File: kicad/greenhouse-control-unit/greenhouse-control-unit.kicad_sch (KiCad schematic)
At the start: 69 parts, among them J1 Pluggable_Terminal_01x02, J10 Molex_KK-254_01x10, J10_LittleBuck1 Conn_01x01_Female, J11_LittleBuck1 Conn_01x01_Female, J12_BigBuck1 Conn_01x01_Female, J13_BigBuck1 Conn_01x01_Female, J14_LittleBuck1 Conn_01x01_Female, J15_LittleBuck1 Conn_01x01_Female, J2 Pluggable_Terminal_01x02, J3 Pluggable_Terminal_01x02, J4 Molex_KK-254_01x08, J5 Conn_01x10_Female, J6 Conn_01x10_Female, J6_BigBuck1 Conn_01x01_Female, J7 Conn_01x15_Female, J7_BigBuck1 Conn_01x01_Female, J8 Conn_01x15_Female, J9 Molex_KK-396_01x16, Q1 2N7000, Q10 IRLB8721PBF, Q11 IRLB8721PBF, Q2 2N7000, Q3 2N7000, Q4 IRLB8721PBF, Q5 IRLB8721PBF, Q6 IRLB8721PBF, Q7 IRLB8721PBF, Q8 IRLB8721PBF, Q9 IRLB8721PBF, U1 74HC595, U2 74HC595

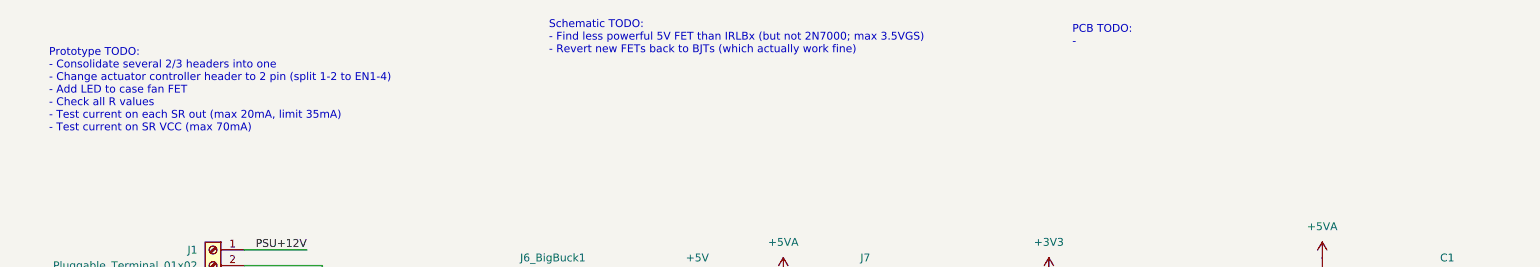
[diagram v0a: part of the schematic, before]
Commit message: Updated TODO's to use 2N7x's properly
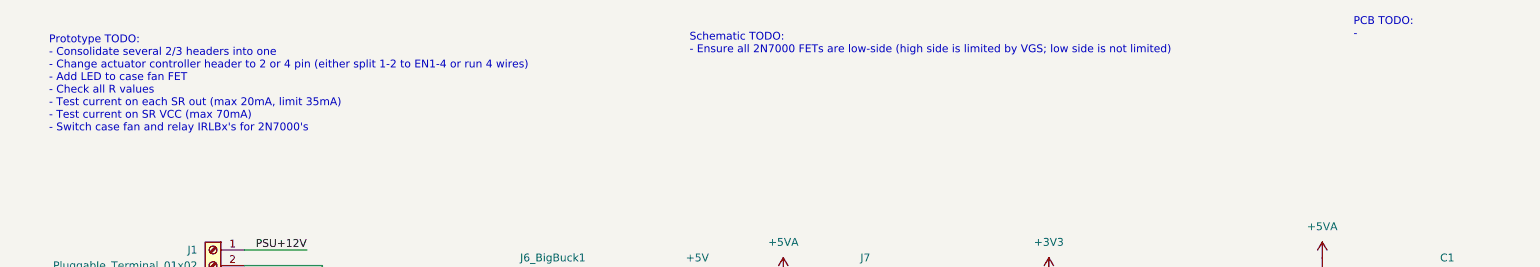
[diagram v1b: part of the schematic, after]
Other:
- note added: "Prototype TODO: - Consolidate several 2/3 headers into one - Change actuator controller header to 2 or 4 pin (either split 1-2 to EN1-4 or run 4 wires) - Add LED to case fan FET - Check all R values - Test current on each SR out (max 20mA, limit 35mA) - Test current on SR VCC (max 70mA) - Switch case fan and relay IRLBx's for 2N7000's"
- note added: "Schematic TODO: - Ensure all 2N7000 FETs are low-side (high side is limited by VGS; low side is not limited)"
- note removed: "Prototype TODO: - Consolidate several 2/3 headers into one - Change actuator controller header to 2 pin (split 1-2 to EN1-4) - Add LED to case fan FET - Check all R values - Test current on each SR out (max 20mA, limit 35mA) - Test current on SR VCC (max 70mA)"
- note removed: "Schematic TODO: - Find less powerful 5V FET than IRLBx (but not 2N7000; max 3.5VGS) - Revert new FETs back to BJTs (which actually work fine)"
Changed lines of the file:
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@@
     (effects (font (size 1.27 1.27)) (justify left bottom))
   )
-  (text "PCB TODO:\n- " (at 193.04 22.86 0)
+  (text "PCB TODO:\n- " (at 238.76 21.59 0)
     (effects (font (size 1.27 1.27)) (justify left bottom))
   )
@@
     (effects (font (size 1.27 1.27)) (justify left bottom))
   )
-  (text "Schematic TODO:\n- Find less powerful 5V FET than IRLBx (but not 2N7000; max 3.5VGS)\n- Revert new FETs back to BJTs (which actually work fine)"
-    (at 107.95 24.13 0)
+  (text "Schematic TODO:\n- Ensure all 2N7000 FETs are low-side (high side is limited by VGS; low side is not limited)\n"
+    (at 130.81 24.13 0)
     (effects (font (size 1.27 1.27)) (justify left bottom))
   )
-  (text "Prototype TODO:\n- Consolidate several 2/3 headers into one\n- Change actuator controller header to 2 pin (split 1-2 to EN1-4)\n- Add LED to case fan FET\n- Check all R values\n- Test current on each SR out (max 20mA, limit 35mA)\n- Test current on SR VCC (max 70mA)"
+  (text "Prototype TODO:\n- Consolidate several 2/3 headers into one\n- Change actuator controller header to 2 or 4 pin (either split 1-2 to EN1-4 or run 4 wires)\n- Add LED to case fan FET\n- Check all R values\n- Test current on each SR out (max 20mA, limit 35mA)\n- Test current on SR VCC (max 70mA)\n- Switch case fan and relay IRLBx's for 2N7000's"
     (at 26.67 36.83 0)
     (effects (font (size 1.27 1.27)) (justify left bottom))

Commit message: Update TODO and ignore file
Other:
- note added: "Schematic TODO: - Ensure all 2N7000 FETs are low-side (high side is limited by VGS; low side is not limited) - Resistors on SR inputs to prevent parasite power? Maybe make diode redundant?"
- note removed: "Schematic TODO: - Ensure all 2N7000 FETs are low-side (high side is limited by VGS; low side is not limited)"
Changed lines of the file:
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@@
     (effects (font (size 1.27 1.27)) (justify left bottom))
   )
-  (text "PCB TODO:\n- " (at 238.76 21.59 0)
+  (text "PCB TODO:\n- " (at 240.03 24.13 0)
     (effects (font (size 1.27 1.27)) (justify left bottom))
   )
@@
     (effects (font (size 1.27 1.27)) (justify left bottom))
   )
-  (text "Schematic TODO:\n- Ensure all 2N7000 FETs are low-side (high side is limited by VGS; low side is not limited)\n"
-    (at 130.81 24.13 0)
+  (text "Schematic TODO: \n- Ensure all 2N7000 FETs are low-side (high side is limited by VGS; low side is not limited)\n- Resistors on SR inputs to prevent parasite power? Maybe make diode redundant?"
+    (at 132.08 26.67 0)
     (effects (font (size 1.27 1.27)) (justify left bottom))
   )
@@
     )
   )
-  (symbol (lib_id "power:+5V") (at 120.65 217.17 0) (unit 1)
-    (in_bom yes) (on_board yes) (fields_autoplaced)
-    (property "Reference" "#PWR07" (id 0) (at 120.65 220.98 0)
-      (effects (font (size 1.27 1.27)) hide)
-    )
-    (property "Value" "+5V" (id 1) (at 120.65 212.09 0))
-    (property "Footprint" "" (id 2) (at 120.65 217.17 0)
-      (effects (font (size 1.27 1.27)) hide)
-    )
-    (property "Datasheet" "" (id 3) (at 120.65 217.17 0)
-      (effects (font (size 1.27 1.27)) hide)
-    )
-    (pin "1")
-  )
   (symbol (lib_id "power:GND") (at 233.68 243.84 0) (unit 1)
     (in_bom yes) (on_board yes) (fields_autoplaced)
@@
     (pin "2")
   )
+  (symbol (lib_id "power:+5V") (at 120.65 217.17 0) (unit 1)
+    (in_bom yes) (on_board yes) (fields_autoplaced)
+    (property "Reference" "#PWR?" (id 0) (at 120.65 220.98 0)
+      (effects (font (size 1.27 1.27)) hide)
+    )
+    (property "Value" "+5V" (id 1) (at 120.65 212.09 0))
+    (property "Footprint" "" (id 2) (at 120.65 217.17 0)
+      (effects (font (size 1.27 1.27)) hide)
+    )
+    (property "Datasheet" "" (id 3) (at 120.65 217.17 0)
+      (effects (font (size 1.27 1.27)) hide)
+    )
+    (pin "1")
+  )
   (symbol (lib_id "power:+3V3") (at 189.23 59.69 0) (unit 1)
     (in_bom yes) (on_board yes) (fields_autoplaced)
@@
       (reference "#PWR06") (unit 1) (value "GND") (footprint "")
     )
-    (path "/270b5206-01f6-4326-bca0-f1b215f9f6ac"
-      (reference "#PWR07") (unit 1) (value "+5V") (footprint "")
-    )
     (path "/14624e4f-3e7f-43e4-90a1-bcd722e8b790"
       (reference "#PWR08") (unit 1) (value "+5V") (footprint "")
@@
       (reference "#PWR044") (unit 1) (value "+12V") (footprint "")
     )
+    (path "/b3a04bcd-a8de-4fd3-afa7-99bb35daab3f"
+      (reference "#PWR?") (unit 1) (value "+5V") (footprint "")
+    )
     (path "/e9cc145f-bccc-4781-862a-a53065926266"

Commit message: New schematic for L298N motor driver
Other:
- added sheet L298N motor driver (L298N-motor-driver.kicad_sch)
- note added: "Prototype TODO: - Check all R values - Test current on each SR out (max 20mA, limit 35mA) - Test current on SR VCC (max 70mA) - Add EN transistor for SR - Add L298 to main board"
- note added: "Schematic TODO: - Disable SR when no input voltage using transistor - Change beep FET back to BJT 2N2222A"
- note removed: "Prototype TODO: - Consolidate several 2/3 headers into one - Change actuator controller header to 2 or 4 pin (either split 1-2 to EN1-4 or run 4 wires) - Add LED to case fan FET - Check all R values - Test current on each SR out (max 20mA, limit 35mA) - Test current on SR VCC (max 70mA) - Switch case fan and relay IRLBx's for 2N7000's"
- note removed: "Schematic TODO: - Ensure all 2N7000 FETs are low-side (high side is limited by VGS; low side is not limited) - Resistors on SR inputs to prevent parasite power? Maybe make diode redundant?"
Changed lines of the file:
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@@
   (junction (at 95.25 238.76) (diameter 0) (color 0 0 0 0)
   )
-  (junction (at 104.14 171.45) (diameter 0) (color 0 0 0 0)
-  )
   (junction (at 295.91 151.13) (diameter 0) (color 0 0 0 0)
   )
@@
     (stroke (width 0) (type default) (color 0 0 0 0))
   )
-  (wire (pts (xy 104.14 171.45) (xy 125.73 171.45))
+  (wire (pts (xy 86.36 171.45) (xy 125.73 171.45))
     (stroke (width 0) (type default) (color 0 0 0 0))
   )
@@
     (stroke (width 0) (type default) (color 0 0 0 0))
   )
-  (wire (pts (xy 104.14 173.99) (xy 104.14 171.45))
-    (stroke (width 0) (type default) (color 0 0 0 0))
-  )
   (wire (pts (xy 259.08 64.77) (xy 259.08 67.31))
     (stroke (width 0) (type default) (color 0 0 0 0))
@@
     (stroke (width 0) (type default) (color 0 0 0 0))
   )
-  (wire (pts (xy 125.73 173.99) (xy 104.14 173.99))
-    (stroke (width 0) (type default) (color 0 0 0 0))
-  )
   (wire (pts (xy 104.14 177.8) (xy 125.73 177.8))
     (stroke (width 0) (type default) (color 0 0 0 0))
@@
     (stroke (width 0) (type default) (color 0 0 0 0))
   )
-  (wire (pts (xy 86.36 171.45) (xy 104.14 171.45))
-    (stroke (width 0) (type default) (color 0 0 0 0))
-  )
   (wire (pts (xy 365.76 127) (xy 365.76 128.27))
     (stroke (width 0) (type default) (color 0 0 0 0))
@@
     (effects (font (size 1.27 1.27)) (justify left bottom))
   )
-  (text "Schematic TODO: \n- Ensure all 2N7000 FETs are low-side (high side is limited by VGS; low side is not limited)\n- Resistors on SR inputs to prevent parasite power? Maybe make diode redundant?"
+  (text "Schematic TODO: \n- Disable SR when no input voltage using transistor\n- Change beep FET back to BJT 2N2222A"
     (at 132.08 26.67 0)
     (effects (font (size 1.27 1.27)) (justify left bottom))
   )
-  (text "Prototype TODO:\n- Consolidate several 2/3 headers into one\n- Change actuator controller header to 2 or 4 pin (either split 1-2 to EN1-4 or run 4 wires)\n- Add LED to case fan FET\n- Check all R values\n- Test current on each SR out (max 20mA, limit 35mA)\n- Test current on SR VCC (max 70mA)\n- Switch case fan and relay IRLBx's for 2N7000's"
+  (text "Prototype TODO:\n- Check all R values\n- Test current on each SR out (max 20mA, limit 35mA)\n- Test current on SR VCC (max 70mA)\n- Add EN transistor for SR\n- Add L298 to main board"
     (at 26.67 36.83 0)
     (effects (font (size 1.27 1.27)) (justify left bottom))
@@
     (effects (font (size 1.27 1.27)) (justify left bottom))
   )
-  (label "Motor_ENA" (at 125.73 173.99 180)
-    (effects (font (size 1.27 1.27)) (justify right bottom))
-  )
   (label "SW4_SR_Q12" (at 318.77 74.93 0)
     (effects (font (size 1.27 1.27)) (justify left bottom))
@@
   (symbol (lib_id "power:+5V") (at 120.65 217.17 0) (unit 1)
     (in_bom yes) (on_board yes) (fields_autoplaced)
-    (property "Reference" "#PWR?" (id 0) (at 120.65 220.98 0)
+    (property "Reference" "#PWR0101" (id 0) (at 120.65 220.98 0)
       (effects (font (size 1.27 1.27)) hide)
     )
@@
     (pin "3")
   )
+  (sheet (at 339.09 198.12) (size 58.42 35.56) (fields_autoplaced)
+    (stroke (width 0.1524) (type solid) (color 0 0 0 0))
+    (fill (color 0 0 0 0.0000))
+    (property "Sheet name" "L298N motor driver" (id 0) (at 339.09 197.4084 0)
+      (effects (font (size 1.27 1.27)) (justify left bottom))
+    )
+    (property "Sheet file" "L298N-motor-driver.kicad_sch" (id 1) (at 339.09 234.2646 0)
+      (effects (font (size 1.27 1.27)) (justify left top))
+    )
+  )
   (sheet_instances
     (path "/" (page "1"))
+    (path "/c8388099-9606-46b9-9f66-ad2ea4b72ec6" (page "2"))
   )
   (symbol_instances
@@
     )
     (path "/b3a04bcd-a8de-4fd3-afa7-99bb35daab3f"
-      (reference "#PWR?") (unit 1) (value "+5V") (footprint "")
+      (reference "#PWR0101") (unit 1) (value "+5V") (footprint "")
+    )
+    (path "/c8388099-9606-46b9-9f66-ad2ea4b72ec6/621d562f-1ba8-4a7e-bf1a-6add68c1e5fa"
+      (reference "#PWR0102") (unit 1) (value "GND") (footprint "")
+    )
+    (path "/c8388099-9606-46b9-9f66-ad2ea4b72ec6/d9226e02-c0d4-4875-9a90-5ff655385a42"
+      (reference "#PWR0103") (unit 1) (value "GND") (footprint "")
+    )
+    (path "/c8388099-9606-46b9-9f66-ad2ea4b72ec6/ffee6268-c691-4fee-8d07-2fcf704786b8"
+      (reference "#PWR0104") (unit 1) (value "+5V") (footprint "")
+    )
+    (path "/c8388099-9606-46b9-9f66-ad2ea4b72ec6/3bedd05b-2dac-4928-b481-4e94d1fc07be"
+      (reference "#PWR0105") (unit 1) (value "GND") (footprint "")
+    )
+    (path "/c8388099-9606-46b9-9f66-ad2ea4b72ec6/e33ec384-03d4-42a8-b060-0079d3f02614"
+      (reference "#PWR0106") (unit 1) (value "+12V") (footprint "")
+    )
+    (path "/c8388099-9606-46b9-9f66-ad2ea4b72ec6/b4befb27-4008-4e19-8558-ea6bfc08fe0d"
+      (reference "#PWR0107") (unit 1) (value "+5V") (footprint "")
+    )
+    (path "/c8388099-9606-46b9-9f66-ad2ea4b72ec6/0597cceb-f32b-48b0-8822-f08dc77b019a"
+      (reference "#PWR0108") (unit 1) (value "GND") (footprint "")
+    )
+    (path "/c8388099-9606-46b9-9f66-ad2ea4b72ec6/f8349e20-f50b-409d-b70f-d46b045c76a3"
+      (reference "#PWR0109") (unit 1) (value "+12V") (footprint "")
     )
     (path "/e9cc145f-bccc-4781-862a-a53065926266"
@@
       (reference "C2") (unit 1) (value "0.01 μf") (footprint "Capacitor_THT:C_Disc_D3.0mm_W1.6mm_P2.50mm")
     )
+    (path "/c8388099-9606-46b9-9f66-ad2ea4b72ec6/04ce182a-7abb-4f82-b92f-59beb92690a5"
+      (reference "C3") (unit 1) (value "220uF") (footprint "Capacitor_THT:CP_Radial_D6.3mm_P2.50mm")
+    )
+    (path "/c8388099-9606-46b9-9f66-ad2ea4b72ec6/7c8d7a17-2fa6-4a81-860c-670099d2c8f9"
+      (reference "C4") (unit 1) (value "100nF") (footprint "Capacitor_THT:C_Disc_D4.7mm_W2.5mm_P5.00mm")
+    )
+    (path "/c8388099-9606-46b9-9f66-ad2ea4b72ec6/e8027441-943e-46b8-a56c-711fcc5b269f"
+      (reference "C5") (unit 1) (value "100nF") (footprint "Capacitor_THT:C_Disc_D4.7mm_W2.5mm_P5.00mm")
+    )
     (path "/84dea478-b855-4267-aa24-6b336fbce1d8"
       (reference "D1") (unit 1) (value "DSB20I15PA Schottky") (footprint "Package_TO_SOT_THT:TO-220-2_Vertical")
@@
       (reference "D8") (unit 1) (value "LED") (footprint "LED_THT:LED_D5.0mm")
     )
+    (path "/c8388099-9606-46b9-9f66-ad2ea4b72ec6/aea877f5-0ed7-43d1-8662-bec20709999f"
+      (reference "D9") (unit 1) (value "1N4007") (footprint "Diode_THT:D_DO-41_SOD81_P10.16mm_Horizontal")
+    )
+    (path "/c8388099-9606-46b9-9f66-ad2ea4b72ec6/64212f15-f75f-481f-a6fe-64e98eee845a"
+      (reference "D10") (unit 1) (value "1N4007") (footprint "Diode_THT:D_DO-41_SOD81_P10.16mm_Horizontal")
+    )
+    (path "/c8388099-9606-46b9-9f66-ad2ea4b72ec6/eda1c1a0-9fb6-4e29-8fb5-2e3604d67388"
+      (reference "D11") (unit 1) (value "1N4007") (footprint "Diode_THT:D_DO-41_SOD81_P10.16mm_Horizontal")
+    )
+    (path "/c8388099-9606-46b9-9f66-ad2ea4b72ec6/16ee782e-9fd5-4603-9bb2-92bb586f1c40"
+      (reference "D12") (unit 1) (value "1N4007") (footprint "Diode_THT:D_DO-41_SOD81_P10.16mm_Horizontal")
+    )
+    (path "/c8388099-9606-46b9-9f66-ad2ea4b72ec6/d9cd62f5-388a-4f78-9896-4f46b1d54a35"
+      (reference "D13") (unit 1) (value "1N4007") (footprint "Diode_THT:D_DO-41_SOD81_P10.16mm_Horizontal")
+    )
+    (path "/c8388099-9606-46b9-9f66-ad2ea4b72ec6/2838e4ff-3b56-4a56-b1f9-7cb3f296a134"
+      (reference "D14") (unit 1) (value "1N4007") (footprint "Diode_THT:D_DO-41_SOD81_P10.16mm_Horizontal")
+    )
+    (path "/c8388099-9606-46b9-9f66-ad2ea4b72ec6/2c9fd049-fac2-42d1-9903-3c6e2d83b458"
+      (reference "D15") (unit 1) (value "1N4007") (footprint "Diode_THT:D_DO-41_SOD81_P10.16mm_Horizontal")
+    )
+    (path "/c8388099-9606-46b9-9f66-ad2ea4b72ec6/a4b1d692-2142-4886-95dd-72809a8d03ed"
+      (reference "D16") (unit 1) (value "1N4007") (footprint "Diode_THT:D_DO-41_SOD81_P10.16mm_Horizontal")
+    )
     (path "/e0ff723e-9da4-419a-9b7c-537137a1c661"
       (reference "H1") (unit 1) (value "MountingHole") (footprint "MountingHole:MountingHole_3mm")
@@
       (reference "R7") (unit 1) (value "2k") (footprint "Resistor_THT:R_Axial_DIN0207_L6.3mm_D2.5mm_P7.62mm_Horizontal")
     )
+    (path "/c8388099-9606-46b9-9f66-ad2ea4b72ec6/a1d7204f-9437-49c2-b0ae-6481b6a6c9ff"
+      (reference "R8") (unit 1) (value "10k") (footprint "Resistor_THT:R_Axial_DIN0204_L3.6mm_D1.6mm_P5.08mm_Horizontal")
+    )
     (path "/48f1e3b1-710a-42d1-bfff-ca44e51fda44"
       (reference "R9") (unit 1) (value "4k6") (footprint "Resistor_THT:R_Axial_DIN0207_L6.3mm_D2.5mm_P7.62mm_Horizontal")
@@
       (reference "R22") (unit 1) (value "10k") (footprint "Resistor_THT:R_Axial_DIN0204_L3.6mm_D1.6mm_P5.08mm_Horizontal")
     )
+    (path "/c8388099-9606-46b9-9f66-ad2ea4b72ec6/dc1a26b3-6693-4318-93ff-873bee3b6601"
+      (reference "R23") (unit 1) (value "10k") (footprint "Resistor_THT:R_Axial_DIN0204_L3.6mm_D1.6mm_P5.08mm_Horizontal")
+    )
     (path "/9c6824f3-5657-45c3-b20c-8450c4b95d0e"
       (reference "U1") (unit 1) (value "74HC595") (footprint "Package_DIP:DIP-16_W7.62mm_Socket")
@@
       (reference "U2") (unit 1) (value "74HC595") (footprint "Package_DIP:DIP-16_W7.62mm_Socket")
     )
+    (path "/c8388099-9606-46b9-9f66-ad2ea4b72ec6/d4e68898-a7da-4bc4-94ee-4c4d1d1bda8c"
+      (reference "U3") (unit 1) (value "L298HN") (footprint "Package_TO_SOT_THT:TO-220-15_P2.54x2.54mm_StaggerOdd_Lead4.58mm_Vertical")
+    )
   )

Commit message: Changed buzzer FET back to BJT
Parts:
- removed Q3: 2N7000, Package_TO_SOT_THT:TO-92_Inline, symbol Transistor_FET:2N7000
- added Q3: 2N2222A, Package_TO_SOT_THT:TO-92_Inline, symbol Nick:2N2222A
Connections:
- net +5V: now also Q3.3 (C); no longer BZ1.1 (-), D5.2 (A)
- net GND: now also BZ1.2 (+), D5.1 (K)
- net StartBeep_SR_Q1: now also Q3.2 (B)
- net at R11.2: now also D5.2 (A); no longer R12.2
- net at R11.1: now also R12.1, Q3.1 (E); no longer D5.1 (K)
- new net: BZ1.1 (-), R12.2

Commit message: Updated TODO
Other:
- note added: "Schematic TODO: - Disable SR when no input voltage (SR can draw power from inputs; i.e. MC)"
- note removed: "Schematic TODO: - Disable SR when no input voltage using transistor - Change beep FET back to BJT 2N2222A"
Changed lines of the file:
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@@
     (effects (font (size 1.27 1.27)) (justify left bottom))
   )
-  (text "Schematic TODO: \n- Disable SR when no input voltage using transistor\n- Change beep FET back to BJT 2N2222A"
+  (text "Schematic TODO: \n- Disable SR when no input voltage (SR can draw power from inputs; i.e. MC)"
     (at 132.08 26.67 0)
     (effects (font (size 1.27 1.27)) (justify left bottom))
